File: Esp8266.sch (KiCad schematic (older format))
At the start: 32 parts, among them P1 AUTO-PROGRAM JUMPER, P2 CONN_02X10, P3 LiPo, P5 OLED_I2C, P6 USB Serial, SW1 RESET, U1 SPX1117, U2 MCP73831, U3 ESP-12E

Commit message: Version 007-121215
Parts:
- removed R13: 10, symbol R
- added D?: 1N4148, symbol D
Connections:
- net TX: now also D?.1 (K)
- net at P6.3 (P3): now also D?.2 (A)
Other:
- note removed: "NOTA: No se si la OLED \ntiene ya las Pullup"
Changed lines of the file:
@@
 Sheet 2 3
 Title "BadgeInventorsCon"
-Date "2015-12-07"
-Rev "0.06"
+Date "2015-12-12"
+Rev "0.07"
 Comp "The Inventor's House"
 Comment1 "Andrés Sabas"
@@
 	1    0    0    -1
 $EndComp
-Text Notes 9350 2850 0    60   ~ 0
-NOTA: No se si la OLED \ntiene ya las Pullup
 $Comp
 L CONN_01X06 P6
@@
 	1    0    0    -1
 $EndComp
-$Comp
-L R R13
-U 1 1 566774F4
-P 9500 4100
-F 0 "R13" V 9580 4100 50  0000 C CNN
-F 1 "10" V 9500 4100 50  0000 C CNN
-F 2 "" V 9430 4100 30  0000 C CNN
-F 3 "" H 9500 4100 30  0000 C CNN
-	1    9500 4100
-	0    1    1    0
-$EndComp
 Text Notes 1250 5200 0    60   ~ 0
 3.3V LDO\nMax input: 15V\nMin Input: 4.4V\nMax Current: 800mA
@@
 Text Label 6900 5000 2    60   ~ 0
 GPIO14
+$Comp
+L D D?
+U 1 1 566DDB87
+P 9500 4100
+F 0 "D?" H 9500 4200 50  0000 C CNN
+F 1 "1N4148" H 9450 4250 50  0000 C CNN
+F 2 "" H 9500 4100 60  0000 C CNN
+F 3 "" H 9500 4100 60  0000 C CNN
+F 4 "Maxim" H 9500 4100 60  0001 C CNN "Manufacturer"
+F 5 "+85/-40" H 9500 4100 60  0001 C CNN "Temperatura"
+F 6 "5v" H 9500 4100 60  0001 C CNN "Alimentacion"
+	1    9500 4100
+	1    0    0    -1
+$EndComp
 $EndSCHEMATC

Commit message: Cambio circuito, inicio PCB
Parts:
- removed P2: CONN_02X10, symbol CONN_02X10
- added P22, P23: CONN_01X10, Pin_Headers:Pin_Header_Straight_1x10, symbol CONN_01X10
- C1, C2, C3, C4, C5: footprint (none) -> Capacitors_SMD:C_0805_HandSoldering
- D1: footprint (none) -> LEDs:LED-0603
- D2: footprint (none) -> Diodes_SMD:SOD-123
- D3: footprint (none) -> Diodes_SMD:SOD-323
- D4: footprint (none) -> LEDs:LED-0805
- D5: renamed from D?; footprint (none) -> Diodes_SMD:SOD-323
- LED1: footprint (none) -> Neopix:WS2812B_PP
- P1: footprint (none) -> Pin_Headers:Pin_Header_Straight_1x02
- P3: footprint (none) -> open-project:CONN_JST-2_SMD
- P5: footprint (none) -> Socket_Strips:Socket_Strip_Straight_1x04
- P6: footprint (none) -> Socket_Strips:Socket_Strip_Straight_1x06
- R1, R10, R11, R12, R2, R3, R4, R5, R6, R7, R8, R9: footprint (none) -> Resistors_SMD:R_0805_HandSoldering
- SW1: footprint (none) -> open-project:SW_PUSH_SMD
- U1: footprint (none) -> TO_SOT_Packages_SMD:SOT-223
- U2: footprint (none) -> TO_SOT_Packages_SMD:SOT-23-5
- U3: footprint (none) -> esp:ESP-12E
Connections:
- net +3V3: now also P22.9 (P9)
- net +BATT: now also P23.1 (P1)
- net ADC_IN: now also P22.3 (P3)
- net CH_PD: now also P22.4 (P4)
- net GND: now also P22.1 (P1), P23.10 (P10), P23.5 (P5)
- net GPIO0: now also P22.2 (P2), P23.4 (P4)
- net GPIO12: now also P22.7 (P7)
- net GPIO13: now also P22.8 (P8)
- net GPIO14: now also P22.6 (P6)
- net GPIO15: now also P23.2 (P2)
- net GPIO16: now also P22.5 (P5)
- net GPIO2: now also P23.3 (P3)
- net GPIO4/SDA: now also P23.6 (P6)
- net GPIO5/SCL: now also P23.7 (P7)
- net RX: now also P23.9 (P9)
- net TX: now also P23.8 (P8)
- net VCC: now also P22.10 (P10)

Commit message: PCB v0.01
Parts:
- added SW2: SW_PUSH, open-project:SW_PUSH_SMD, symbol SW_PUSH
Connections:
- net GND: now also P22.2 (P2), SW2.2
- net GPIO0: now also SW2.1; no longer P22.2 (P2)
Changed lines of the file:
@@
 Sheet 2 3
 Title "BadgeInventorsCon"
-Date "2015-12-12"
-Rev "0.07"
+Date "2015-12-16"
+Rev "0.08"
 Comp "The Inventor's House"
 Comment1 "Andrés Sabas"
-Comment2 ""
+Comment2 "Eduardo Contreras "
 Comment3 ""
 Comment4 ""
@@
 Text Label 4200 4500 2    60   ~ 0
 GPIO4/SDA
-Text Label 5450 4800 0    60   ~ 0
-GPIO0
 Text Label 4200 4300 2    60   ~ 0
 GPIO0
@@
 	6200 4900 5200 4900
 Wire Wire Line
-	5200 4800 5450 4800
+	5200 4800 5650 4800
 Wire Wire Line
 	5200 4700 5450 4700
@@
 Wire Wire Line
 	5950 4100 5200 4100
+$Comp
+L SW_PUSH SW2
+U 1 1 56724A25
+P 3100 1700
+F 0 "SW2" H 3250 1810 50  0000 C CNN
+F 1 "SW_PUSH" H 3100 1620 50  0000 C CNN
+F 2 "open-project:SW_PUSH_SMD" H 3100 1700 60  0001 C CNN
+F 3 "" H 3100 1700 60  0000 C CNN
+	1    3100 1700
+	0    -1   -1   0
+$EndComp
+$Comp
+L GND #PWR038
+U 1 1 56724B42
+P 3500 1600
+F 0 "#PWR038" H 3500 1350 50  0001 C CNN
+F 1 "GND" H 3500 1450 50  0000 C CNN
+F 2 "" H 3500 1600 60  0000 C CNN
+F 3 "" H 3500 1600 60  0000 C CNN
+	1    3500 1600
+	1    0    0    -1
+$EndComp
+Wire Wire Line
+	3100 1400 3100 1150
+Wire Wire Line
+	3100 1150 3500 1150
+Wire Wire Line
+	3500 1150 3500 1600
+Wire Wire Line
+	3100 2000 3100 2150
+Connection ~ 3100 2150
+Wire Wire Line
+	5650 4800 5650 4900
+Connection ~ 5650 4900
 $EndSCHEMATC

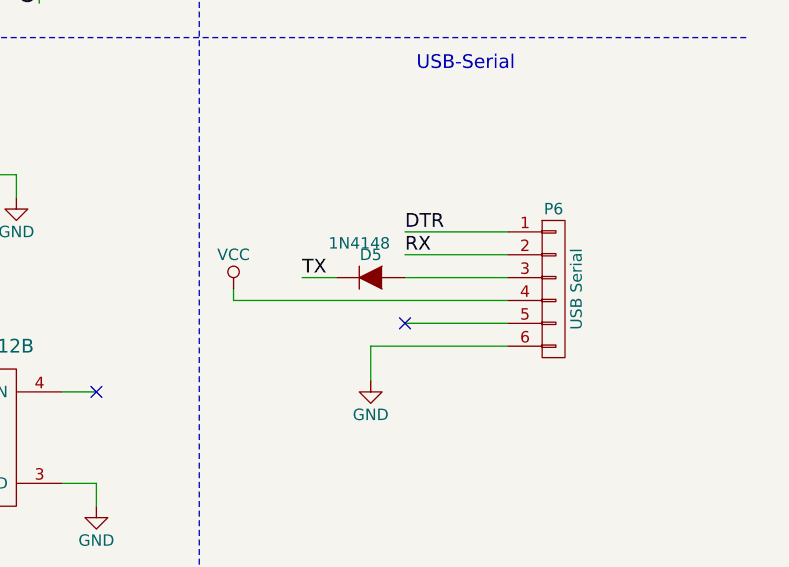
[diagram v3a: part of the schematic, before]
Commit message: Agregado pinout, correccion diodo TX
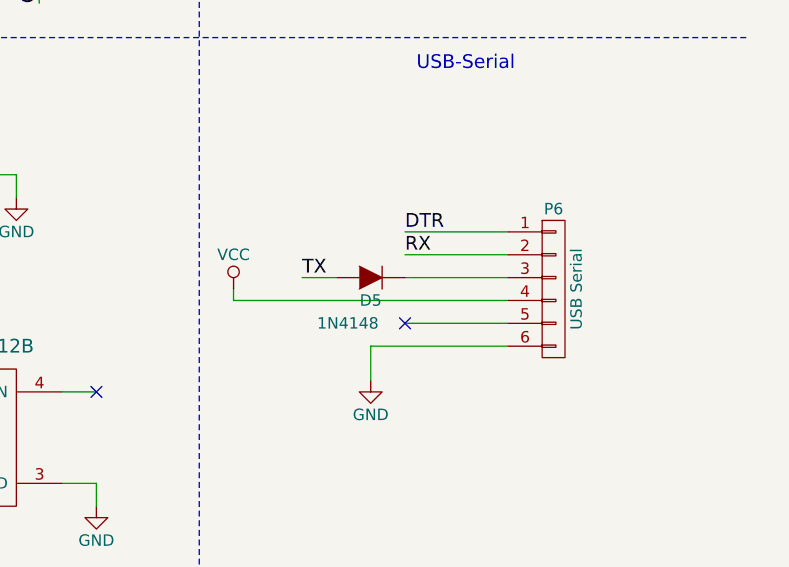
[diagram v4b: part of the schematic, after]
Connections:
- net TX: now also D5.2 (A); no longer D5.1 (K)
- net at P6.3 (P3): now also D5.1 (K); no longer D5.2 (A)
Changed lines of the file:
@@
 	10100 4000 9650 4000
-Wire Wire Line
-	10100 4100 9650 4100
 Wire Wire Line
 	8900 4200 10100 4200
@@
 Wire Wire Line
 	8900 4150 8900 4200
-Wire Wire Line
-	9350 4100 9200 4100
 Wire Wire Line
 	7150 4600 6900 4600
@@
 P 9500 4100
 F 0 "D5" H 9500 4200 50  0000 C CNN
-F 1 "1N4148" H 9450 4250 50  0000 C CNN
+F 1 "1N4148" H 9600 4300 50  0000 C CNN
 F 2 "Diodes_SMD:SOD-323" H 9500 4100 60  0001 C CNN
 F 3 "" H 9500 4100 60  0000 C CNN
@@
 F 6 "5v" H 9500 4100 60  0001 C CNN "Alimentacion"
 	1    9500 4100
-	1    0    0    -1
+	-1   0    0    1
 $EndComp
 $Comp
@@
 	5650 4800 5650 4900
 Connection ~ 5650 4900
+Wire Wire Line
+	9650 4100 10100 4100
+Wire Wire Line
+	9200 4100 9350 4100
 $EndSCHEMATC
